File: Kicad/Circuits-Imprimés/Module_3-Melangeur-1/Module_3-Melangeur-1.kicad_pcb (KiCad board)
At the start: 2 copper layers, 14 parts, among them J1 Conn_01x02, J2 Conn_01x02, J3 Conn_01x02, J4 Conn_01x02, T1 Transformateur, T2 Transformateur, U1 EMRS-1, U2 MD-108

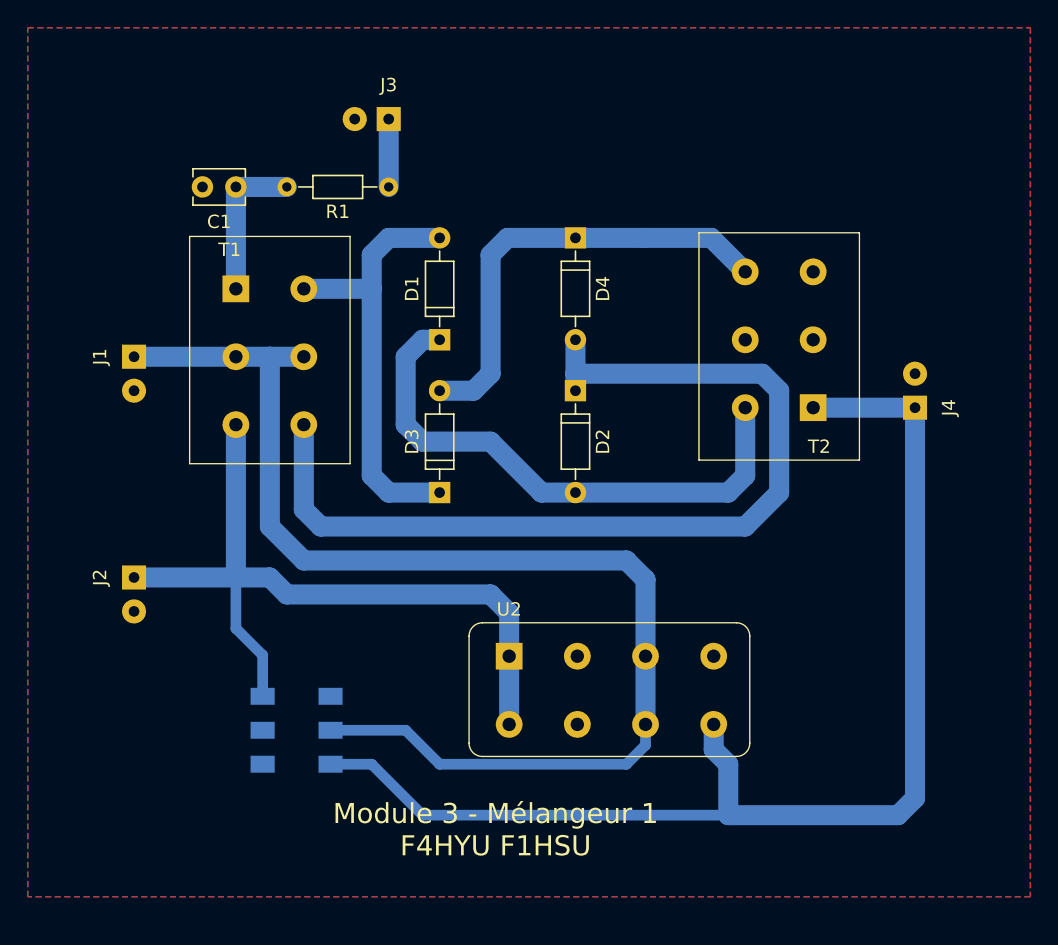
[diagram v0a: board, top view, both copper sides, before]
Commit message: Update hole to the module 3 RF Mixer
 Update Hole for the module 3 - RF Mixer
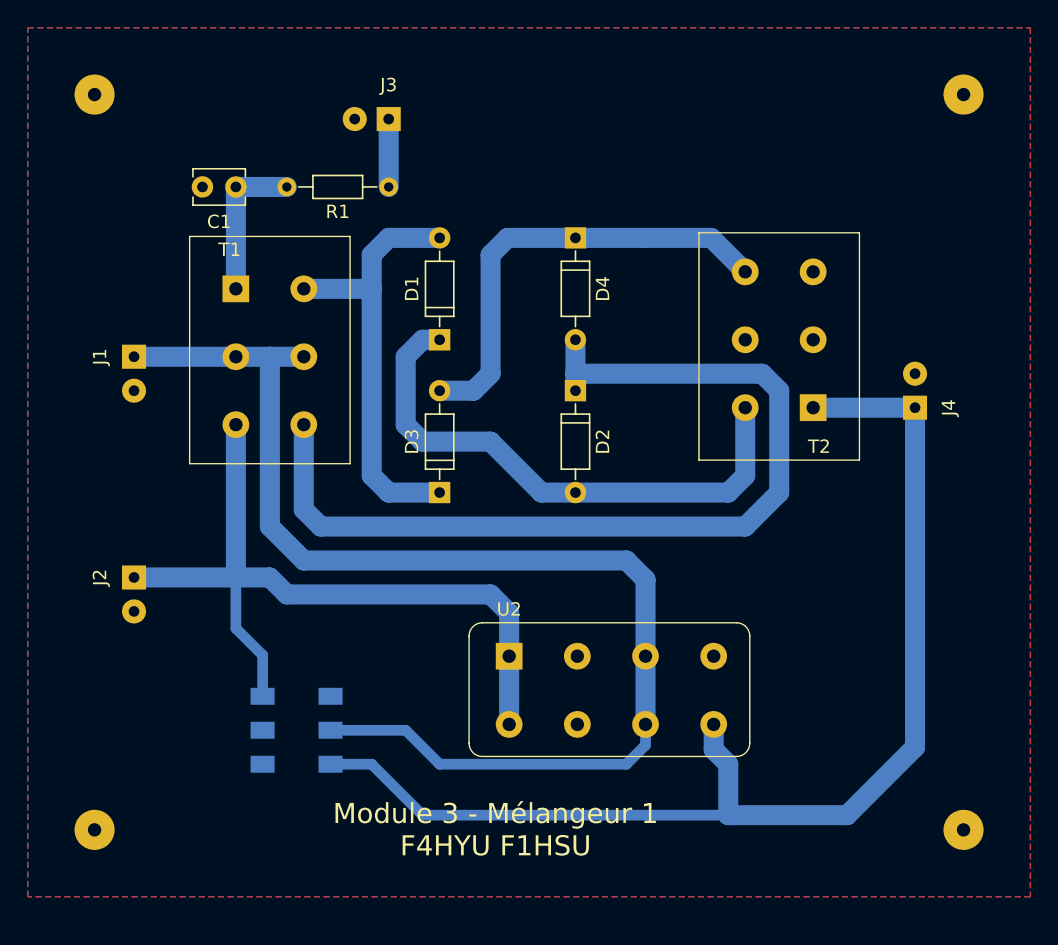
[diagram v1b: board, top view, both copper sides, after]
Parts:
- added REF**: M3-Hole, Visserie-Trous-Modules:M3-Hole, F.Cu at (105.0, 35.0)
- added REF**: M3-Hole, Visserie-Trous-Modules:M3-Hole, F.Cu at (170.0, 35.0)
- added REF**: M3-Hole, Visserie-Trous-Modules:M3-Hole, F.Cu at (170.0, 90.0)
- added REF**: M3-Hole, Visserie-Trous-Modules:M3-Hole, F.Cu at (105.0, 90.0)
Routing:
- net Rf: track 89.9 -> 87.7 mm
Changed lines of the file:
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@@
     (tracks 72)
     (zones 0)
-    (modules 14)
+    (modules 18)
     (nets 11)
   )
@@
   )
   (setup
-    (last_trace_width 0.8)
+    (last_trace_width 0.25)
     (user_trace_width 0.8)
     (user_trace_width 1.5)
@@
     (pad_to_mask_clearance 0.2)
     (aux_axis_origin 0 0)
-    (visible_elements FFFFFF7F)
+    (visible_elements 7FFFFFFF)
     (pcbplotparams
       (layerselection 0x01000_80000001)
@@
     )
   )
+  (module Visserie-Trous-Modules:M3-Hole (layer F.Cu)
+    (at 105 35)
+    (fp_text reference REF** (at 0 2.54) (layer F.SilkS) hide
+      (effects (font (size 1 1) (thickness 0.15)))
+    )
+    (fp_text value M3-Hole (at 0.635 -2.54) (layer F.Fab) hide
+      (effects (font (size 1 1) (thickness 0.15)))
+    )
+    (pad 1 thru_hole circle (at 0 0) (size 3 3) (drill 1) (layers *.Cu *.Mask))
+  )
+  (module Visserie-Trous-Modules:M3-Hole (layer F.Cu)
+    (at 170 35)
+    (fp_text reference REF** (at 0 2.54) (layer F.SilkS) hide
+      (effects (font (size 1 1) (thickness 0.15)))
+    )
+    (fp_text value M3-Hole (at 0.635 -2.54) (layer F.Fab) hide
+      (effects (font (size 1 1) (thickness 0.15)))
+    )
+    (pad 1 thru_hole circle (at 0 0) (size 3 3) (drill 1) (layers *.Cu *.Mask))
+  )
+  (module Visserie-Trous-Modules:M3-Hole (layer F.Cu)
+    (at 170 90)
+    (fp_text reference REF** (at 0 2.54) (layer F.SilkS) hide
+      (effects (font (size 1 1) (thickness 0.15)))
+    )
+    (fp_text value M3-Hole (at 0.635 -2.54) (layer F.Fab) hide
+      (effects (font (size 1 1) (thickness 0.15)))
+    )
+    (pad 1 thru_hole circle (at 0 0) (size 3 3) (drill 1) (layers *.Cu *.Mask))
+  )
+  (module Visserie-Trous-Modules:M3-Hole (layer F.Cu)
+    (at 105 90)
+    (fp_text reference REF** (at 0 2.54) (layer F.SilkS) hide
+      (effects (font (size 1 1) (thickness 0.15)))
+    )
+    (fp_text value M3-Hole (at 0.635 -2.54) (layer F.Fab) hide
+      (effects (font (size 1 1) (thickness 0.15)))
+    )
+    (pad 1 thru_hole circle (at 0 0) (size 3 3) (drill 1) (layers *.Cu *.Mask))
+  )
   (gr_text "Module 3 - Mélangeur 1\nF4HYU F1HSU" (at 135 90) (layer F.SilkS)
     (effects (font (size 1.5 1.5) (thickness 0.3)))
@@
   (segment (start 115.57 41.91) (end 115.57 49.53) (width 1.5) (layer B.Cu) (net 1))
   (segment (start 119.38 41.91) (end 115.57 41.91) (width 1.5) (layer B.Cu) (net 1))
-  (segment (start 130.81 53.34) (end 129.54 53.34) (width 1.5) (layer B.Cu) (net 3) (status 400000))
-  (segment (start 138.43 64.77) (end 140.97 64.77) (width 1.5) (layer B.Cu) (net 3) (status 800000))
+  (segment (start 130.81 53.34) (end 129.54 53.34) (width 1.5) (layer B.Cu) (net 3))
+  (segment (start 138.43 64.77) (end 140.97 64.77) (width 1.5) (layer B.Cu) (net 3))
   (segment (start 134.62 60.96) (end 138.43 64.77) (width 1.5) (layer B.Cu) (net 3))
   (segment (start 129.54 60.96) (end 134.62 60.96) (width 1.5) (layer B.Cu) (net 3))
@@
   (segment (start 128.27 54.61) (end 128.27 59.69) (width 1.5) (layer B.Cu) (net 3))
   (segment (start 129.54 53.34) (end 128.27 54.61) (width 1.5) (layer B.Cu) (net 3))
-  (segment (start 153.67 58.42) (end 153.67 63.5) (width 1.5) (layer B.Cu) (net 3) (status 400000))
-  (segment (start 152.4 64.77) (end 140.97 64.77) (width 1.5) (layer B.Cu) (net 3) (status 800000))
+  (segment (start 153.67 58.42) (end 153.67 63.5) (width 1.5) (layer B.Cu) (net 3))
+  (segment (start 152.4 64.77) (end 140.97 64.77) (width 1.5) (layer B.Cu) (net 3))
   (segment (start 153.67 63.5) (end 152.4 64.77) (width 1.5) (layer B.Cu) (net 3))
   (segment (start 125.73 49.53) (end 120.65 49.53) (width 1.5) (layer B.Cu) (net 4))
@@
   (segment (start 127 45.72) (end 125.73 46.99) (width 1.5) (layer B.Cu) (net 4))
   (segment (start 140.97 55.88) (end 154.94 55.88) (width 1.5) (layer B.Cu) (net 5))
-  (segment (start 120.65 66.04) (end 120.65 59.69) (width 1.5) (layer B.Cu) (net 5) (status 800000))
+  (segment (start 120.65 66.04) (end 120.65 59.69) (width 1.5) (layer B.Cu) (net 5))
   (segment (start 121.92 67.31) (end 120.65 66.04) (width 1.5) (layer B.Cu) (net 5))
   (segment (start 153.67 67.31) (end 121.92 67.31) (width 1.5) (layer B.Cu) (net 5))
@@
   (segment (start 156.21 57.15) (end 156.21 64.77) (width 1.5) (layer B.Cu) (net 5))
   (segment (start 154.94 55.88) (end 156.21 57.15) (width 1.5) (layer B.Cu) (net 5))
-  (segment (start 140.97 53.34) (end 140.97 55.88) (width 1.5) (layer B.Cu) (net 5) (status 400000))
+  (segment (start 140.97 53.34) (end 140.97 55.88) (width 1.5) (layer B.Cu) (net 5))
   (segment (start 140.97 55.88) (end 140.97 57.15) (width 1.5) (layer B.Cu) (net 5))
-  (segment (start 140.97 45.72) (end 135.89 45.72) (width 1.5) (layer B.Cu) (net 6) (status 400000))
-  (segment (start 133.35 57.15) (end 130.81 57.15) (width 1.5) (layer B.Cu) (net 6) (status 800000))
+  (segment (start 140.97 45.72) (end 135.89 45.72) (width 1.5) (layer B.Cu) (net 6))
+  (segment (start 133.35 57.15) (end 130.81 57.15) (width 1.5) (layer B.Cu) (net 6))
   (segment (start 134.62 55.88) (end 133.35 57.15) (width 1.5) (layer B.Cu) (net 6))
   (segment (start 134.62 46.99) (end 134.62 55.88) (width 1.5) (layer B.Cu) (net 6))
@@
   (segment (start 136.01 77.01) (end 136.01 82.11) (width 1.5) (layer B.Cu) (net 8))
   (segment (start 127 36.83) (end 127 41.91) (width 1.5) (layer B.Cu) (net 9))
-  (segment (start 122.65 85.09) (end 125.73 85.09) (width 0.8) (layer B.Cu) (net 10) (status 400000))
+  (segment (start 122.65 85.09) (end 125.73 85.09) (width 0.8) (layer B.Cu) (net 10))
   (segment (start 129.54 88.9) (end 152.4 88.9) (width 0.8) (layer B.Cu) (net 10))
   (segment (start 125.73 85.09) (end 129.54 88.9) (width 0.8) (layer B.Cu) (net 10))
   (segment (start 158.75 58.42) (end 166.37 58.42) (width 1.5) (layer B.Cu) (net 10))
   (segment (start 151.31 82.11) (end 151.31 84) (width 1.5) (layer B.Cu) (net 10))
-  (segment (start 166.37 87.63) (end 166.37 58.42) (width 1.5) (layer B.Cu) (net 10))
-  (segment (start 165.1 88.9) (end 166.37 87.63) (width 1.5) (layer B.Cu) (net 10))
-  (segment (start 152.4 88.9) (end 165.1 88.9) (width 1.5) (layer B.Cu) (net 10))
+  (segment (start 166.37 83.82) (end 166.37 58.42) (width 1.5) (layer B.Cu) (net 10) (status 800000))
+  (segment (start 161.29 88.9) (end 166.37 83.82) (width 1.5) (layer B.Cu) (net 10))
+  (segment (start 152.4 88.9) (end 161.29 88.9) (width 1.5) (layer B.Cu) (net 10))
   (segment (start 152.4 85.09) (end 152.4 88.9) (width 1.5) (layer B.Cu) (net 10))
   (segment (start 151.31 84) (end 152.4 85.09) (width 1.5) (layer B.Cu) (net 10))

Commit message: Update wrong cuting ouside
Updage cuting outside in module 3
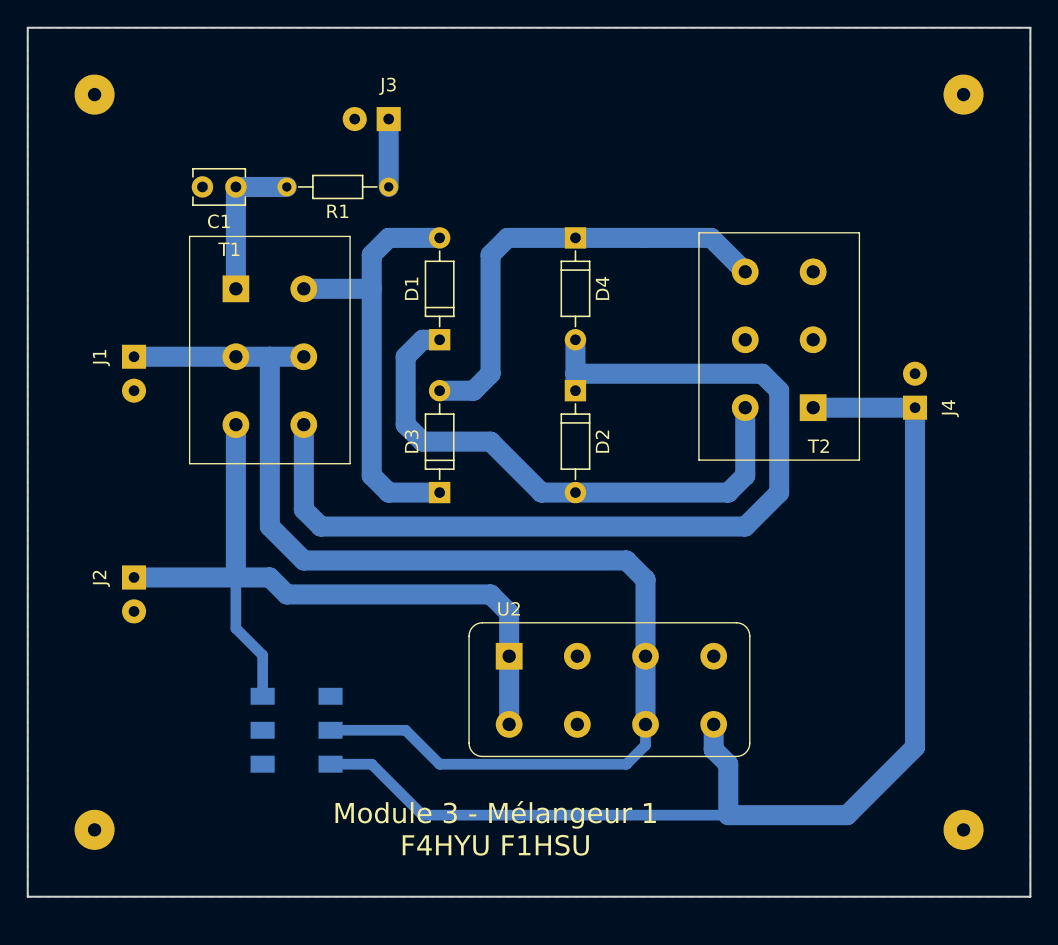
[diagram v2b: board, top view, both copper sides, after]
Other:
- board outline added: 75 x 65 mm
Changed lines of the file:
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@@
     (pad 1 thru_hole circle (at 0 0) (size 3 3) (drill 1) (layers *.Cu *.Mask))
   )
+  (gr_line (start 100 95) (end 100 30) (angle 90) (layer Edge.Cuts) (width 0.15))
+  (gr_line (start 175 95) (end 100 95) (angle 90) (layer Edge.Cuts) (width 0.15))
+  (gr_line (start 175 30) (end 175 95) (angle 90) (layer Edge.Cuts) (width 0.15))
+  (gr_line (start 100 30) (end 175 30) (angle 90) (layer Edge.Cuts) (width 0.15))
   (gr_text "Module 3 - Mélangeur 1\nF4HYU F1HSU" (at 135 90) (layer F.SilkS)
     (effects (font (size 1.5 1.5) (thickness 0.3)))
   )
-  (gr_line (start 100 95) (end 100 30) (angle 90) (layer Eco2.User) (width 0.2))
-  (gr_line (start 175 95) (end 100 95) (angle 90) (layer Eco2.User) (width 0.2))
-  (gr_line (start 175 30) (end 175 95) (angle 90) (layer Eco2.User) (width 0.2))
-  (gr_line (start 100 30) (end 175 30) (angle 90) (layer Eco2.User) (width 0.2))
   (segment (start 115.57 41.91) (end 115.57 49.53) (width 1.5) (layer B.Cu) (net 1))
   (segment (start 119.38 41.91) (end 115.57 41.91) (width 1.5) (layer B.Cu) (net 1))
@@
   (segment (start 158.75 58.42) (end 166.37 58.42) (width 1.5) (layer B.Cu) (net 10))
   (segment (start 151.31 82.11) (end 151.31 84) (width 1.5) (layer B.Cu) (net 10))
-  (segment (start 166.37 83.82) (end 166.37 58.42) (width 1.5) (layer B.Cu) (net 10) (status 800000))
+  (segment (start 166.37 83.82) (end 166.37 58.42) (width 1.5) (layer B.Cu) (net 10))
   (segment (start 161.29 88.9) (end 166.37 83.82) (width 1.5) (layer B.Cu) (net 10))
   (segment (start 152.4 88.9) (end 161.29 88.9) (width 1.5) (layer B.Cu) (net 10))

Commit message: Update Module 3 Optimise GND
Update Module 3:
New GND Optimised in PCB Bottom
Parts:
- moved D1 2.54 mm to (130.8, 50.8)
- moved J2 2.54 mm to (108.0, 68.6)
- moved T2 2.54 mm to (156.2, 50.8)
- moved C1 2.54 mm to (115.6, 39.4)
- moved D2 2.54 mm to (141.0, 54.6)
- moved D3 2.54 mm to (130.8, 62.2)
- moved D4 2.54 mm to (141.0, 43.2)
- moved J1 2.54 mm to (108.0, 52.1)
- moved J3 2.54 mm to (127.0, 34.3)
- moved J4 2.54 mm to (166.4, 55.9)
- moved R1 2.54 mm to (127.0, 39.4)
- moved T1 2.54 mm to (118.1, 52.1)
- moved U1 1.27 mm to (120.7, 83.8)
- moved U2 1.27 mm to (143.5, 81.3)
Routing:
- net Lo: track 58.6 -> 67.0 mm
- net Net-(D2-Pad1): track 70.7 -> 73.5 mm
- net Rf: track 87.7 -> 90.0 mm
- net If: track 92.7 -> 94.3 mm
